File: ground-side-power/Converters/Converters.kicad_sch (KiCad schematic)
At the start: 46 parts, among them J1 DAQ Voltage Sensing, J2 DAQ Current Sensing, J3 Ground Connections, J4 BATT_IN, J5 POWER_OUT, J6 5V_IN, U1 K7805-3AR3, U2 TPS55340, U3 INA180, U4 INA180

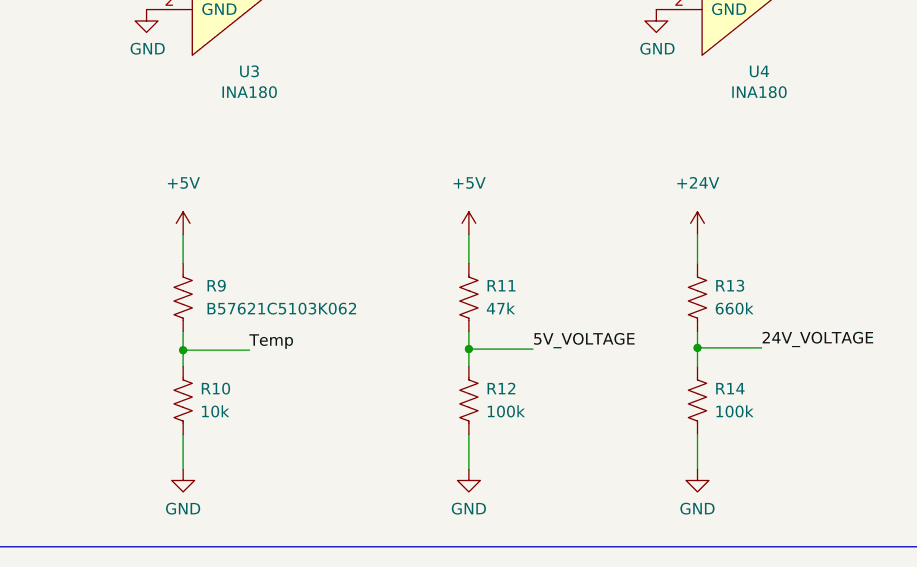
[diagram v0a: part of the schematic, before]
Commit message: fixed drc errors and changed thermistor symbol
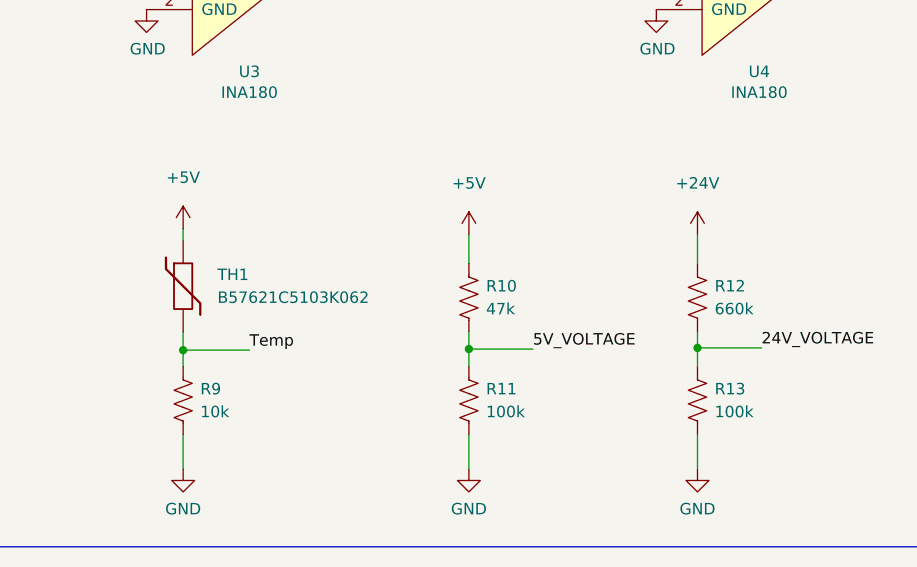
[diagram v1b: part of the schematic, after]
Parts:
- removed R9: B57621C5103K062, Resistor_SMD:R_1206_3216Metric_Pad1.30x1.75mm_HandSolder, symbol Device:R_US
- added TH1: B57621C5103K062, Resistor_SMD:R_1206_3216Metric_Pad1.30x1.75mm_HandSolder, symbol Device:Thermistor
- renumbered R11 to R10, R12 to R11, R13 to R12, R14 to R13, R10 to R9
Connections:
- net +5V: now also TH1.1
- net Temp: now also TH1.2
